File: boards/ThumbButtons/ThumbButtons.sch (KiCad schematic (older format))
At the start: 140 parts

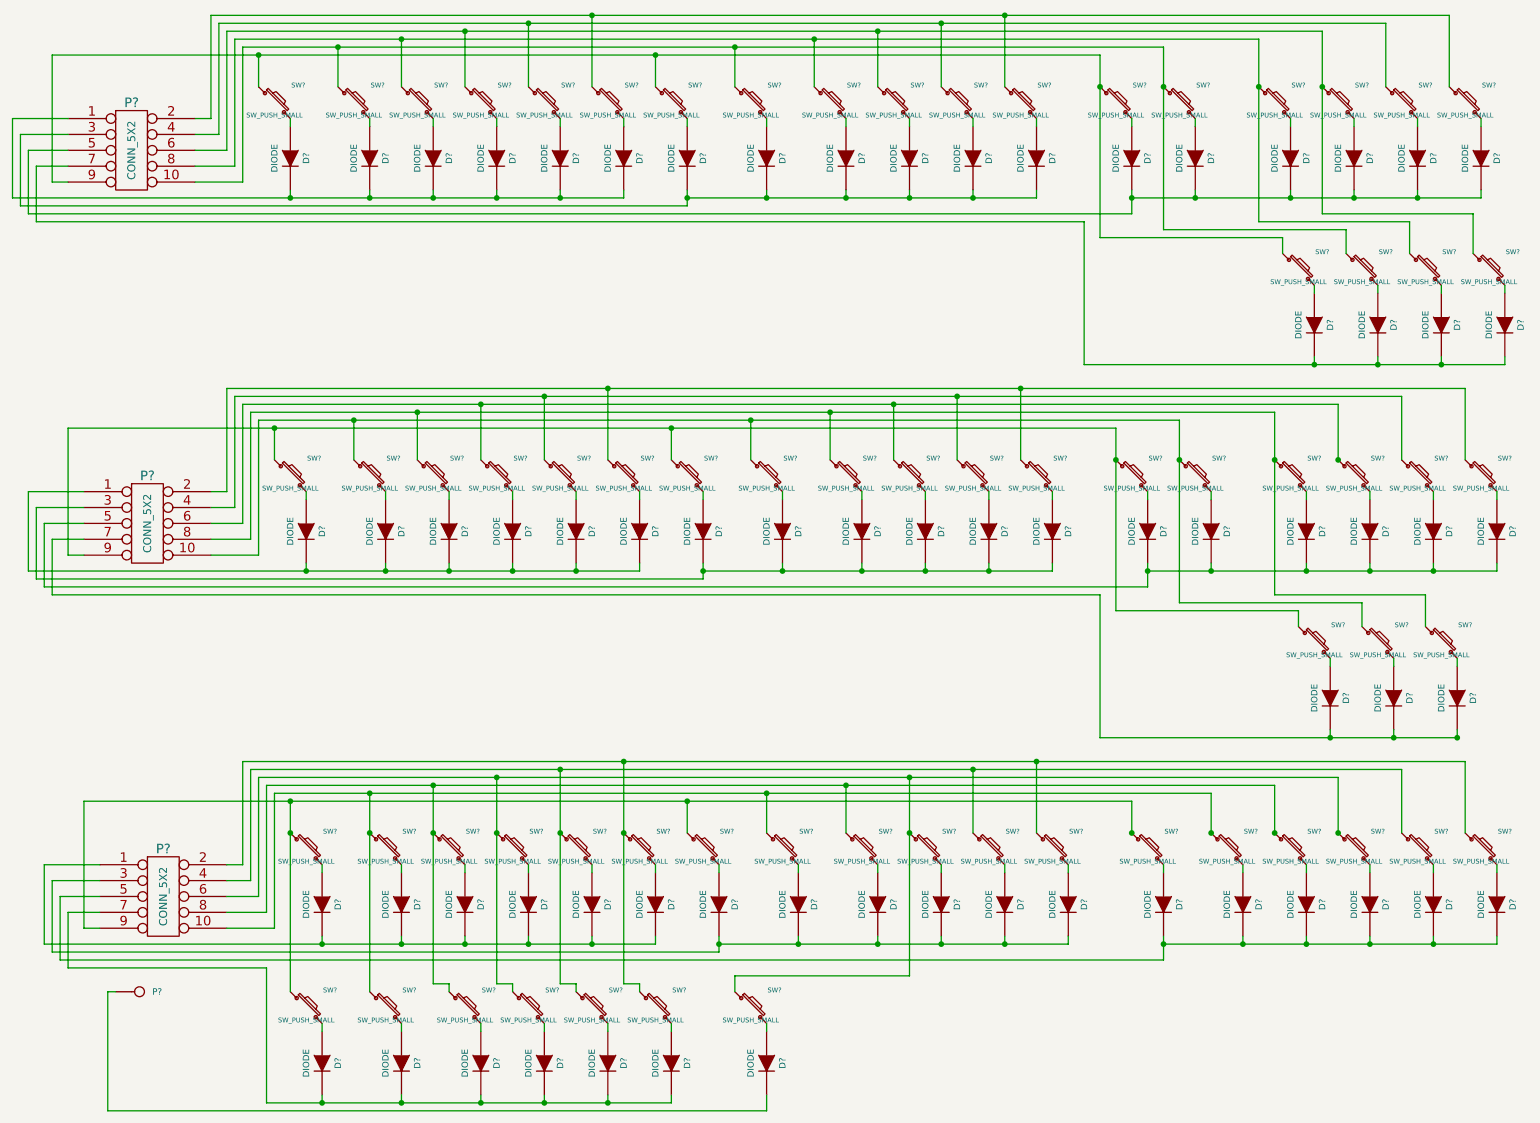
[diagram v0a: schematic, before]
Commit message: Fixed thumb piston wiring schematics
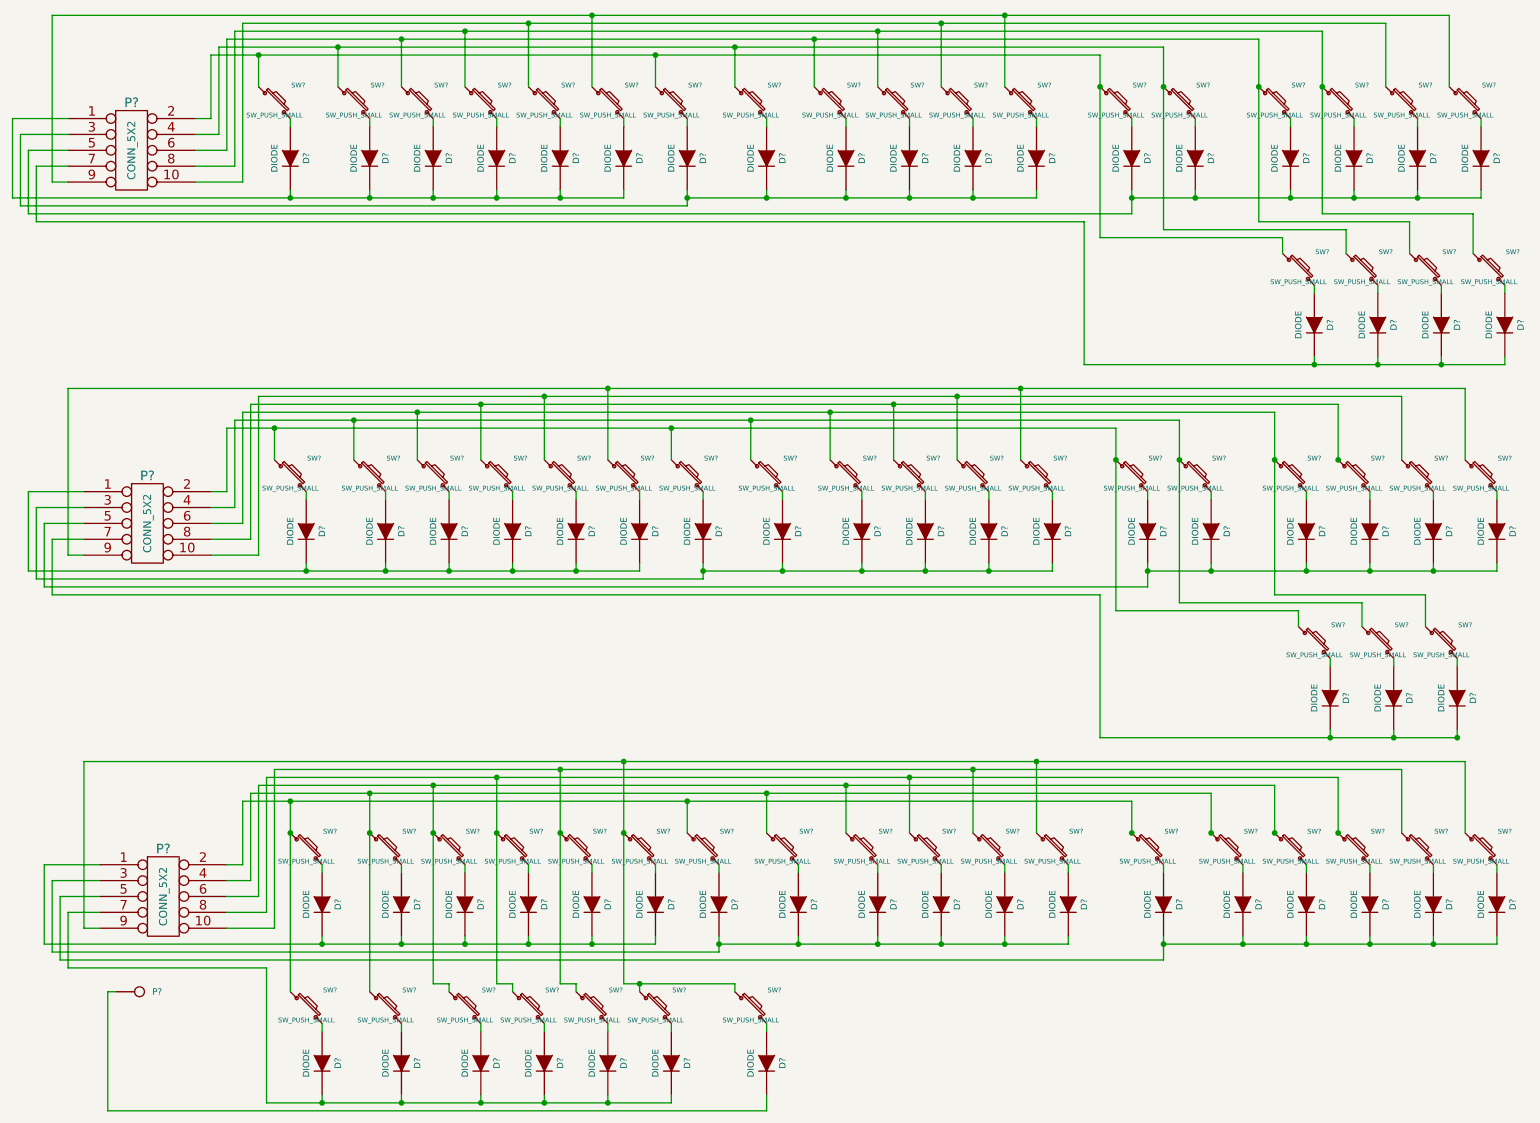
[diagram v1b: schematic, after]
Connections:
- net at SW?.1, SW?.1, SW?.1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: now also P?.4; no longer P?.10 (x3)
- net at SW?.1, SW?.1, SW?.1: now also P?.9; no longer P?.2 (x2)
- net at SW?.1, SW?.1, SW?.1: now also P?.10; no longer P?.4 (x2)
- net at SW?.1, SW?.1, SW?.1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: now also P?.8; no longer P?.6
- net at SW?.1, SW?.1, SW?.1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: now also P?.6; no longer P?.8 (x3)
- net at SW?.1, SW?.1, SW?.1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: now also P?.2; no longer P?.9 (x3)
- net at SW?.1, SW?.1, SW?.1: now also P?.8; no longer P?.6
- net at SW?.1, SW?.1, SW?.1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: now also P?.9, SW?.1; no longer P?.2
- net at SW?.1, SW?.1, SW?.1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: now also P?.10; no longer P?.4
- net at SW?.1, SW?.1, SW?.1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: now also P?.8; no longer P?.6, SW?.1
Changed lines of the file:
@@
 	2250 1150 2250 950
 Wire Wire Line
-	950  950  7550 950
+	1950 950  7550 950
 Wire Wire Line
 	4750 1150 4750 950
@@
 Wire Wire Line
 	1050 1750 950  1750
-Wire Wire Line
-	950  1750 950  950
 Connection ~ 2250 950
 Wire Wire Line
@@
 Connection ~ 8900 2900
 Wire Wire Line
-	1850 1750 2150 1750
-Wire Wire Line
-	2150 1750 2150 900
-Wire Wire Line
-	2150 900  7950 900
+	2150 1750 1850 1750
+Wire Wire Line
+	2000 900  7950 900
 Wire Wire Line
 	2750 900  2750 1150
@@
 	1850 1650 2100 1650
 Wire Wire Line
-	2100 1650 2100 850
-Wire Wire Line
-	2100 850  8550 850
+	2050 850  8550 850
 Wire Wire Line
 	3150 850  3150 1150
@@
 	1850 1550 2050 1550
 Wire Wire Line
-	2050 1550 2050 800
-Wire Wire Line
-	2050 800  8950 800
+	2100 800  8950 800
 Wire Wire Line
 	3550 800  3550 1150
@@
 	1850 1450 2000 1450
 Wire Wire Line
-	2000 1450 2000 750
-Wire Wire Line
-	2000 750  9350 750
+	2150 750  9350 750
 Wire Wire Line
 	3950 750  3950 1150
@@
 	1850 1350 1950 1350
 Wire Wire Line
-	1950 1350 1950 700
-Wire Wire Line
-	1950 700  9750 700
+	950  700  9750 700
 Wire Wire Line
 	4350 700  4350 1150
@@
 	2350 3500 2350 3300
 Wire Wire Line
-	1050 3300 7650 3300
+	2050 3300 7650 3300
 Wire Wire Line
 	4850 3500 4850 3300
@@
 Wire Wire Line
 	1150 4100 1050 4100
-Wire Wire Line
-	1050 4100 1050 3300
 Connection ~ 2350 3300
 Wire Wire Line
@@
 	1950 4100 2250 4100
 Wire Wire Line
-	2250 4100 2250 3250
-Wire Wire Line
-	2250 3250 8050 3250
+	2100 3250 8050 3250
 Wire Wire Line
 	2850 3250 2850 3500
@@
 	1950 4000 2200 4000
 Wire Wire Line
-	2200 4000 2200 3200
-Wire Wire Line
-	2200 3200 8650 3200
+	2150 3200 8650 3200
 Wire Wire Line
 	3250 3200 3250 3500
@@
 	1950 3900 2150 3900
 Wire Wire Line
-	2150 3900 2150 3150
-Wire Wire Line
-	2150 3150 9050 3150
+	2200 3150 9050 3150
 Wire Wire Line
 	3650 3150 3650 3500
@@
 	1950 3800 2100 3800
 Wire Wire Line
-	2100 3800 2100 3100
-Wire Wire Line
-	2100 3100 9450 3100
+	2250 3100 9450 3100
 Wire Wire Line
 	4050 3100 4050 3500
@@
 	1950 3700 2050 3700
 Wire Wire Line
-	2050 3700 2050 3050
-Wire Wire Line
-	2050 3050 9850 3050
+	1050 3050 9850 3050
 Wire Wire Line
 	4450 3050 4450 3500
@@
 	2450 5650 2450 6850
 Wire Wire Line
-	1150 5650 7750 5650
-Wire Wire Line
-	4950 5850 4950 5650
+	4950 5650 4950 5850
 Connection ~ 4950 5650
 Wire Wire Line
@@
 	1250 6450 1150 6450
 Wire Wire Line
-	1150 6450 1150 5650
-Connection ~ 2450 5650
-Wire Wire Line
 	1250 6250 1000 6250
 Wire Wire Line
@@
 	2050 6450 2350 6450
 Wire Wire Line
-	2350 6450 2350 5600
-Wire Wire Line
-	2350 5600 8250 5600
+	2200 5600 8250 5600
 Wire Wire Line
 	2950 5600 2950 6850
@@
 	2050 6350 2300 6350
 Wire Wire Line
-	2300 6350 2300 5550
-Wire Wire Line
-	2300 5550 8650 5550
+	2250 5550 8650 5550
 Wire Wire Line
 	3350 5550 3350 6800
@@
 	2050 6250 2250 6250
 Wire Wire Line
-	2250 6250 2250 5500
-Wire Wire Line
-	2250 5500 9050 5500
+	2300 5500 9050 5500
 Wire Wire Line
 	3750 5500 3750 6800
@@
 	2050 6150 2200 6150
 Wire Wire Line
-	2200 6150 2200 5450
-Wire Wire Line
-	2200 5450 9450 5450
+	2350 5450 9450 5450
 Wire Wire Line
 	4150 5450 4150 6800
@@
 	2050 6050 2150 6050
 Wire Wire Line
-	2150 6050 2150 5400
-Wire Wire Line
-	2150 5400 9850 5400
+	1150 5400 9850 5400
 Wire Wire Line
 	4550 5400 4550 6800
@@
 	5950 5550 5950 5850
 Connection ~ 3350 5550
-Wire Wire Line
-	6350 5500 6350 6750
 Connection ~ 3750 5500
 Wire Wire Line
@@
 Connection ~ 4150 5850
 Wire Wire Line
-	4550 6800 4650 6800
+	4550 6800 5250 6800
 Wire Wire Line
 	4650 6800 4650 6850
 Connection ~ 4550 5850
 Wire Wire Line
-	5250 6850 5250 6750
-Wire Wire Line
-	5250 6750 6350 6750
-Connection ~ 6350 5850
+	6350 5500 6350 5850
+Wire Wire Line
+	5250 6800 5250 6850
+Connection ~ 4650 6800
+Wire Wire Line
+	2150 5650 7750 5650
+Wire Wire Line
+	2150 6050 2150 5650
+Connection ~ 2450 5650
+Wire Wire Line
+	2200 6150 2200 5600
+Wire Wire Line
+	2250 6250 2250 5550
+Wire Wire Line
+	2300 6350 2300 5500
+Wire Wire Line
+	2350 6450 2350 5450
+Wire Wire Line
+	1150 6450 1150 5400
+Wire Wire Line
+	2050 3700 2050 3300
+Wire Wire Line
+	2100 3800 2100 3250
+Wire Wire Line
+	2150 3900 2150 3200
+Wire Wire Line
+	2200 4000 2200 3150
+Wire Wire Line
+	2250 4100 2250 3100
+Wire Wire Line
+	1050 4100 1050 3050
+Wire Wire Line
+	1950 1350 1950 950
+Wire Wire Line
+	2000 1450 2000 900
+Wire Wire Line
+	2050 1550 2050 850
+Wire Wire Line
+	950  1750 950  700
+Wire Wire Line
+	2100 1650 2100 800
+Wire Wire Line
+	2150 750  2150 1750
 $EndSCHEMATC

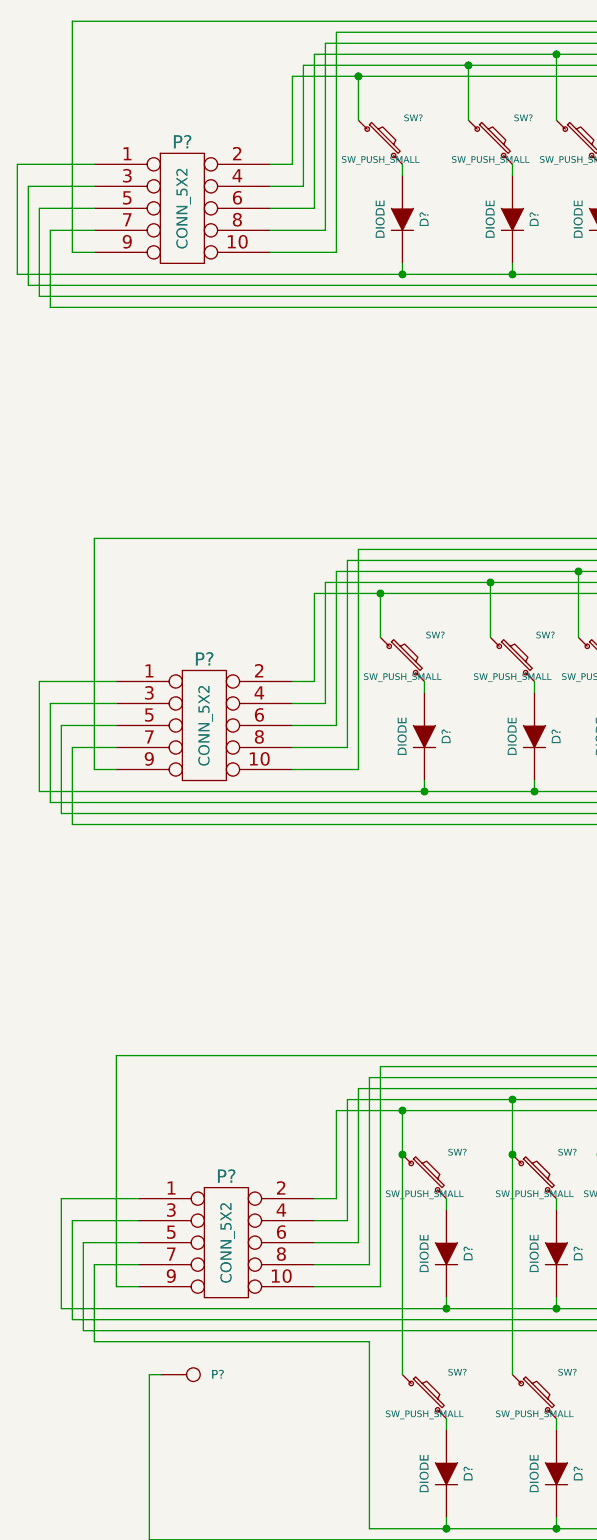
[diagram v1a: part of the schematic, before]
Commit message: First version of thumb encoder schematics
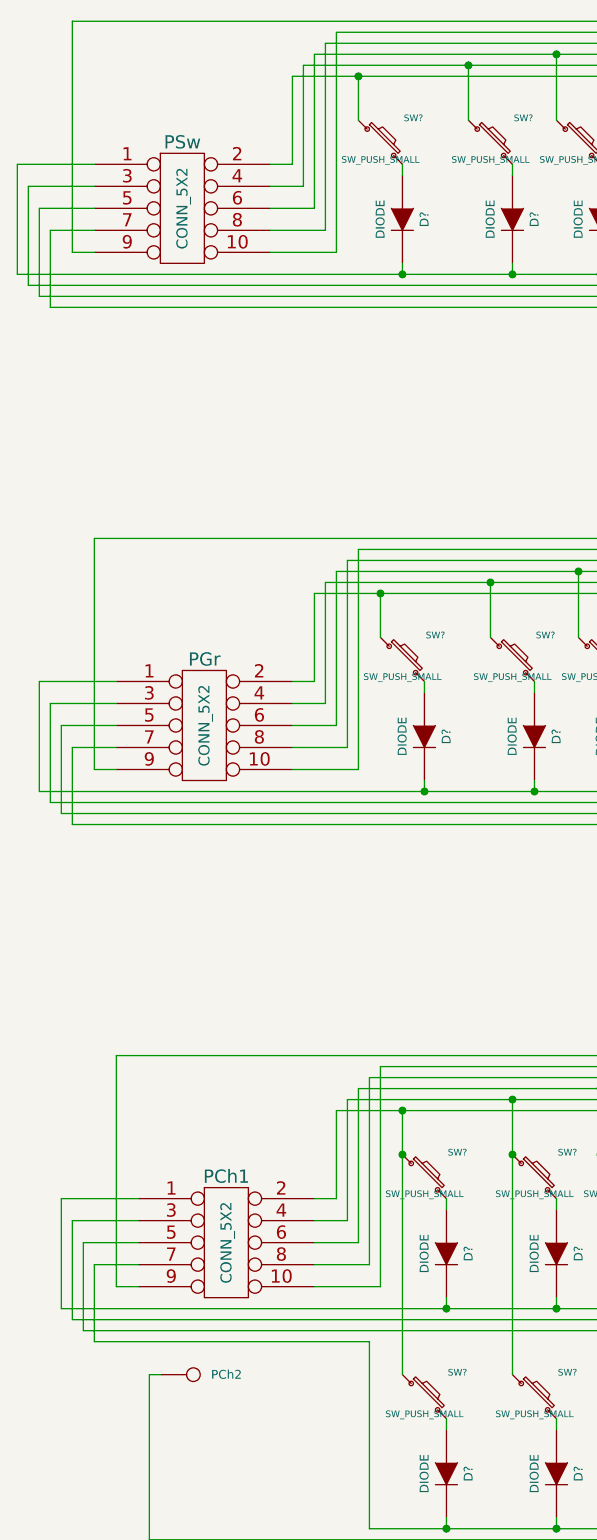
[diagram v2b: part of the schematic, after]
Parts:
- gave numbers to parts that had none: 4
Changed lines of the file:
@@
 $EndDescr
 $Comp
-L CONN_5X2 P?
+L CONN_5X2 PSw
 U 1 1 525B16B2
 P 1450 1550
-F 0 "P?" H 1450 1850 60  0000 C CNN
+F 0 "PSw" H 1450 1850 60  0000 C CNN
 F 1 "CONN_5X2" V 1450 1550 50  0000 C CNN
 F 2 "" H 1450 1550 60  0000 C CNN
@@
 $EndComp
 $Comp
-L CONN_1 P?
+L CONN_1 PCh2
 U 1 1 525B16CD
 P 1500 6850
-F 0 "P?" H 1580 6850 40  0000 L CNN
+F 0 "PCh2" H 1580 6850 40  0000 L CNN
 F 1 "CONN_1" H 1500 6905 30  0001 C CNN
 F 2 "" H 1500 6850 60  0000 C CNN
@@
 Connection ~ 8950 1150
 $Comp
-L CONN_5X2 P?
+L CONN_5X2 PGr
 U 1 1 525B4FB3
 P 1550 3900
-F 0 "P?" H 1550 4200 60  0000 C CNN
+F 0 "PGr" H 1550 4200 60  0000 C CNN
 F 1 "CONN_5X2" V 1550 3900 50  0000 C CNN
 F 2 "" H 1550 3900 60  0000 C CNN
@@
 Connection ~ 9050 3500
 $Comp
-L CONN_5X2 P?
+L CONN_5X2 PCh1
 U 1 1 525B516D
 P 1650 6250
-F 0 "P?" H 1650 6550 60  0000 C CNN
+F 0 "PCh1" H 1650 6550 60  0000 C CNN
 F 1 "CONN_5X2" V 1650 6250 50  0000 C CNN
 F 2 "" H 1650 6250 60  0000 C CNN
